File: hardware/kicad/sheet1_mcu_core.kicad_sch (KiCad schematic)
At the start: 1 part, among them U10 Raspberry_Pi_Pico

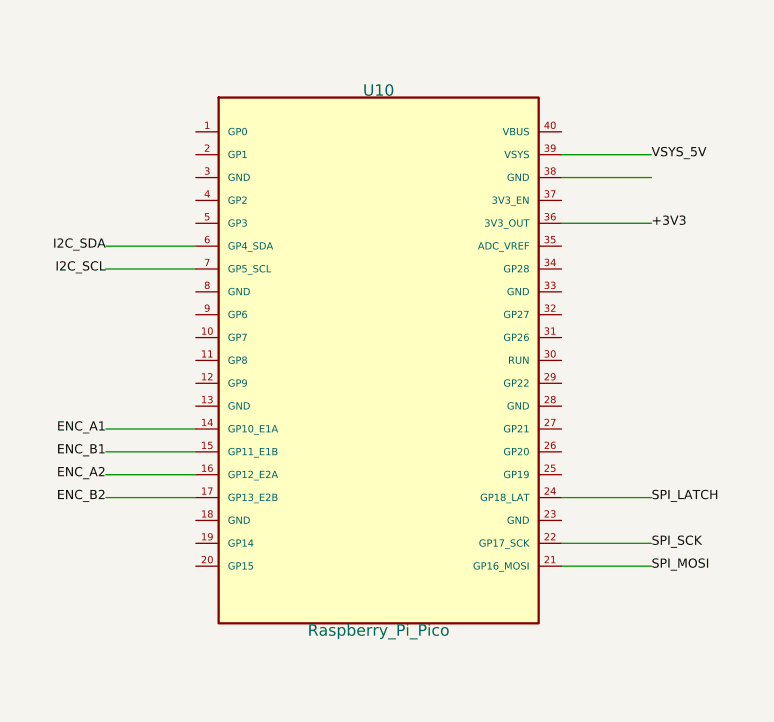
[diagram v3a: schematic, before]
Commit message: Auto-route 392 copper tracks for 64-channel HPVE phased array PCB
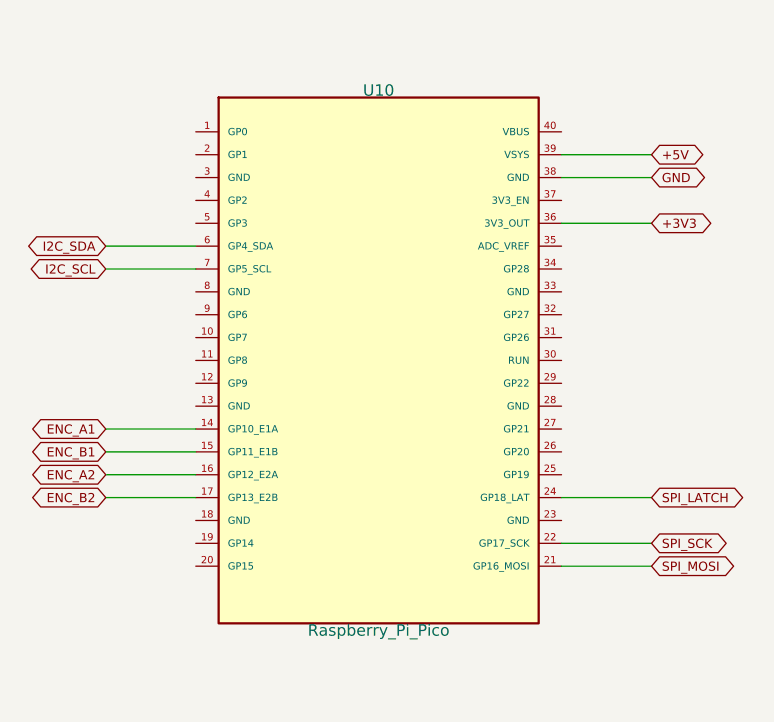
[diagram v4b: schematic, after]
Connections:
- net GND: now reaches U10.38 (GND)
- net VSYS_5V renamed +5V
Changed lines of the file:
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@@
 	)
 	(wire (pts (xy 99.68 77.30) (xy 89.68 77.30)) (stroke (width 0) (type default)) (uuid "{gen_uuid()}"))
-	(label "I2C_SDA" (at 89.68 77.30 180) (effects (font (size 1.016 1.016)) (justify right)) (uuid "{gen_uuid()}"))
+	(global_label "I2C_SDA" (shape bidirectional) (at 89.68 77.30 180) (effects (font (size 1.016 1.016))) (uuid "{gen_uuid()}"))
 	(wire (pts (xy 99.68 79.84) (xy 89.68 79.84)) (stroke (width 0) (type default)) (uuid "{gen_uuid()}"))
-	(label "I2C_SCL" (at 89.68 79.84 180) (effects (font (size 1.016 1.016)) (justify right)) (uuid "{gen_uuid()}"))
+	(global_label "I2C_SCL" (shape bidirectional) (at 89.68 79.84 180) (effects (font (size 1.016 1.016))) (uuid "{gen_uuid()}"))
 	(wire (pts (xy 99.68 97.62) (xy 89.68 97.62)) (stroke (width 0) (type default)) (uuid "{gen_uuid()}"))
-	(label "ENC_A1" (at 89.68 97.62 180) (effects (font (size 1.016 1.016)) (justify right)) (uuid "{gen_uuid()}"))
+	(global_label "ENC_A1" (shape bidirectional) (at 89.68 97.62 180) (effects (font (size 1.016 1.016))) (uuid "{gen_uuid()}"))
 	(wire (pts (xy 99.68 100.16) (xy 89.68 100.16)) (stroke (width 0) (type default)) (uuid "{gen_uuid()}"))
-	(label "ENC_B1" (at 89.68 100.16 180) (effects (font (size 1.016 1.016)) (justify right)) (uuid "{gen_uuid()}"))
+	(global_label "ENC_B1" (shape bidirectional) (at 89.68 100.16 180) (effects (font (size 1.016 1.016))) (uuid "{gen_uuid()}"))
 	(wire (pts (xy 99.68 102.70) (xy 89.68 102.70)) (stroke (width 0) (type default)) (uuid "{gen_uuid()}"))
-	(label "ENC_A2" (at 89.68 102.70 180) (effects (font (size 1.016 1.016)) (justify right)) (uuid "{gen_uuid()}"))
+	(global_label "ENC_A2" (shape bidirectional) (at 89.68 102.70 180) (effects (font (size 1.016 1.016))) (uuid "{gen_uuid()}"))
 	(wire (pts (xy 99.68 105.24) (xy 89.68 105.24)) (stroke (width 0) (type default)) (uuid "{gen_uuid()}"))
-	(label "ENC_B2" (at 89.68 105.24 180) (effects (font (size 1.016 1.016)) (justify right)) (uuid "{gen_uuid()}"))
+	(global_label "ENC_B2" (shape bidirectional) (at 89.68 105.24 180) (effects (font (size 1.016 1.016))) (uuid "{gen_uuid()}"))
 	(wire (pts (xy 140.32 112.86) (xy 150.32 112.86)) (stroke (width 0) (type default)) (uuid "{gen_uuid()}"))
-	(label "SPI_MOSI" (at 150.32 112.86 0) (effects (font (size 1.016 1.016)) (justify left)) (uuid "{gen_uuid()}"))
+	(global_label "SPI_MOSI" (shape bidirectional) (at 150.32 112.86 0) (effects (font (size 1.016 1.016))) (uuid "{gen_uuid()}"))
 	(wire (pts (xy 140.32 110.32) (xy 150.32 110.32)) (stroke (width 0) (type default)) (uuid "{gen_uuid()}"))
-	(label "SPI_SCK" (at 150.32 110.32 0) (effects (font (size 1.016 1.016)) (justify left)) (uuid "{gen_uuid()}"))
+	(global_label "SPI_SCK" (shape bidirectional) (at 150.32 110.32 0) (effects (font (size 1.016 1.016))) (uuid "{gen_uuid()}"))
 	(wire (pts (xy 140.32 105.24) (xy 150.32 105.24)) (stroke (width 0) (type default)) (uuid "{gen_uuid()}"))
-	(label "SPI_LATCH" (at 150.32 105.24 0) (effects (font (size 1.016 1.016)) (justify left)) (uuid "{gen_uuid()}"))
+	(global_label "SPI_LATCH" (shape bidirectional) (at 150.32 105.24 0) (effects (font (size 1.016 1.016))) (uuid "{gen_uuid()}"))
 	(wire (pts (xy 140.32 67.14) (xy 150.32 67.14)) (stroke (width 0) (type default)) (uuid "{gen_uuid()}"))
-	(label "VSYS_5V" (at 150.32 67.14 0) (effects (font (size 1.016 1.016)) (justify left)) (uuid "{gen_uuid()}"))
+	(global_label "+5V" (shape bidirectional) (at 150.32 67.14 0) (effects (font (size 1.016 1.016))) (uuid "{gen_uuid()}"))
 	(wire (pts (xy 140.32 74.76) (xy 150.32 74.76)) (stroke (width 0) (type default)) (uuid "{gen_uuid()}"))
-	(label "+3V3" (at 150.32 74.76 0) (effects (font (size 1.016 1.016)) (justify left)) (uuid "{gen_uuid()}"))
+	(global_label "+3V3" (shape bidirectional) (at 150.32 74.76 0) (effects (font (size 1.016 1.016))) (uuid "{gen_uuid()}"))
 	(wire (pts (xy 140.32 69.68) (xy 150.32 69.68)) (stroke (width 0) (type default)) (uuid "{gen_uuid()}"))
+	(global_label "GND" (shape bidirectional) (at 150.32 69.68 0) (effects (font (size 1.016 1.016))) (uuid "{gen_uuid()}"))
 )
